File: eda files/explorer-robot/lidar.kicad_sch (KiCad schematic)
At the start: 4 parts, among them J6 LID, Q2 AO3400A

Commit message: Add sheet titles and tidy RP2354B schematic layout
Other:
- title: (none) -> LIDAR connector
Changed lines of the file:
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@@
 	(paper "A4")
 	(title_block
+		(title "LIDAR connector")
 		(date "2026-09-27")
 		(rev "v.0.1")

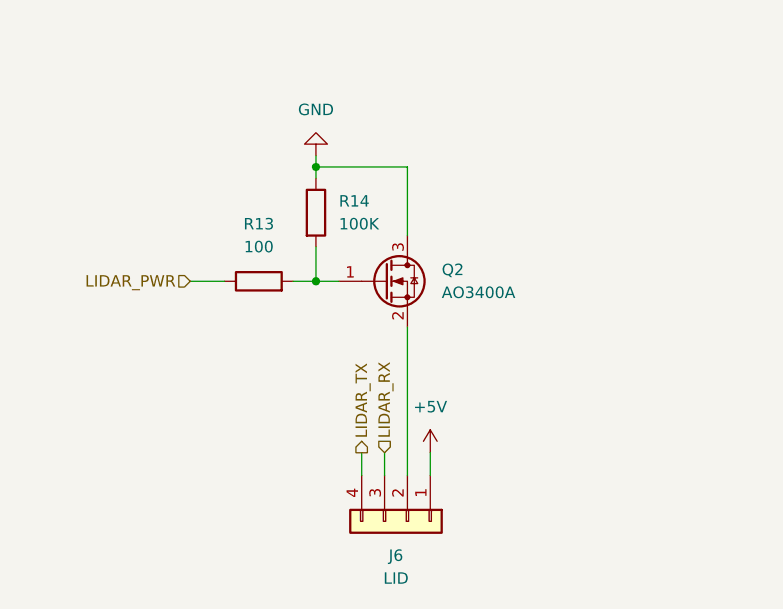
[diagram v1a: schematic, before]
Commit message: Replace power MOSFETs with TPS22917 load switches
Document the switch from low-side MOSFETs to TPS22917 high-side
load switches on the LiDAR and AI camera branches, and add the
expansion connector's switched branch.

Add ADR-0023 requiring each branch's UART to be quiesced and
tri-stated before its power is switched off, to prevent back-feeding
the unpowered load through its ESD diodes.

Rename the `power_mosfet` resource fields to `power_enable`, add
GPIO32 (`EXP_PWR`), and note that the three switched branches can
push the 5 V rail above its continuous current target.
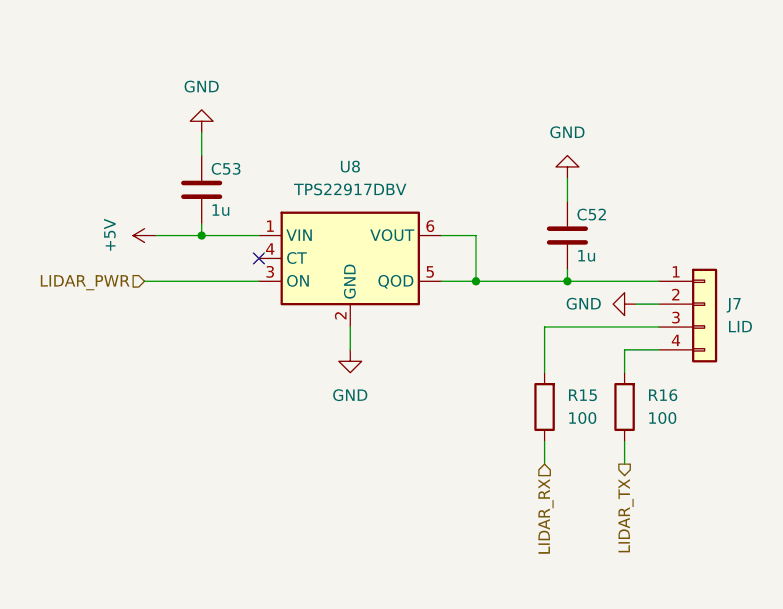
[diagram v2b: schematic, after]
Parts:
- removed J6: LID, Connector_JST:JST_PH_B4B-PH-K_1x04_P2.00mm_Vertical, symbol Connector_Generic:Conn_01x04
- removed Q2: AO3400A, Package_TO_SOT_SMD:SOT-23, symbol Transistor_FET:AO3400A
- removed R13: 100, Resistor_SMD:R_0603_1608Metric, symbol Device:R
- removed R14: 100K, Resistor_SMD:R_0603_1608Metric, symbol Device:R
- added C52, C53: 1u, Capacitor_SMD:C_0603_1608Metric, symbol Device:C
- added J7: LID, Connector_JST:JST_PH_B4B-PH-K_1x04_P2.00mm_Vertical, symbol Connector_Generic:Conn_01x04
- added R15, R16: 100, Resistor_SMD:R_0603_1608Metric, symbol Device:R
- added U8: TPS22917DBV, Package_TO_SOT_SMD:SOT-23-6, symbol Power_Management:TPS22917DBV
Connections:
- net +5V: now also C53.2, U8.1 (VIN)
- net GND: now also C52.1, C53.1, J7.2 (Pin_2), U8.2 (GND)
- net LIDAR_PWR: now also U8.3 (ON)
- net LIDAR_RX: now also R15.1
- net LIDAR_TX: now also R16.1
- new net: J7.4 (Pin_4), R16.2
- new net: C52.2, J7.1 (Pin_1), U8.5 (QOD), U8.6 (VOUT)
- new net: J7.3 (Pin_3), R15.2
- no-connect marks 0 -> 1

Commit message: Add JLCPCB part data for load switch
Also flip BOM sort order to ascending by reference.
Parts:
- U8: JLCPCB_URL (none) -> https://jlcpcb.com/partdetail/TexasInstruments-TPS22917DBVR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; LCSC (none) -> C2681320; MPN (none) -> TPS22917DBVR
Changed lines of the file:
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@@
+			)
+		)
+		(property "JLCPCB_URL" "https://jlcpcb.com/partdetail/TexasInstruments-TPS22917DBVR/C2681320"
+			(at 146.05 88.9 0)
+			(hide yes)
+			(show_name no)
+			(do_not_autoplace no)
+			(effects
+				(font
+					(size 1.27 1.27)
+				)
+			)
+		)
+		(property "LCSC" "C2681320"
+			(at 146.05 88.9 0)
+			(hide yes)
+			(show_name no)
+			(do_not_autoplace no)
+			(effects
+				(font
+					(size 1.27 1.27)
+				)
+			)
+		)
+		(property "MPN" "TPS22917DBVR"
+			(at 146.05 88.9 0)
+			(hide yes)
+			(show_name no)
+			(do_not_autoplace no)
+			(effects
+				(font
+					(size 1.27 1.27)
+				)
 			)
 		)

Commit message: Add R17 current-limiting resistor to lidar schematic
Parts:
- added R17: 100, Resistor_SMD:R_0603_1608Metric, symbol Device:R
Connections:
- net at C52.2, J7.1 (Pin_1), U8.6 (VOUT): now also R17.1; no longer U8.5 (QOD)
- new net: R17.2, U8.5 (QOD)
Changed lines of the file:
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@@
 	)
 	(junction
-		(at 160.02 91.44)
+		(at 165.1 91.44)
 		(diameter 0)
 		(color 0 0 0 0)
@@
 	(wire
 		(pts
-			(xy 156.21 86.36) (xy 160.02 86.36)
+			(xy 156.21 86.36) (xy 165.1 86.36)
 		)
 		(stroke
@@
 	(wire
 		(pts
+			(xy 163.83 91.44) (xy 170.18 91.44)
+		)
+		(stroke
+			(width 0)
+			(type default)
+		)
+	)
+	(wire
+		(pts
 			(xy 170.18 90.17) (xy 170.18 91.44)
 		)
@@
 	(wire
 		(pts
-			(xy 160.02 86.36) (xy 160.02 91.44)
+			(xy 165.1 86.36) (xy 165.1 91.44)
 		)
 		(stroke
@@
 	(wire
 		(pts
-			(xy 160.02 91.44) (xy 156.21 91.44)
-		)
-		(stroke
-			(width 0)
-			(type default)
-		)
-	)
-	(wire
-		(pts
 			(xy 124.46 86.36) (xy 129.54 86.36)
-		)
-		(stroke
-			(width 0)
-			(type default)
-		)
-	)
-	(wire
-		(pts
-			(xy 160.02 91.44) (xy 170.18 91.44)
 		)
 		(stroke
@@
 					(unit 1)
 				)
+			)
+		)
+	)
+	(symbol
+		(lib_id "Device:R")
+		(at 160.02 91.44 270)
+		(unit 1)
+		(body_style 1)
+		(exclude_from_sim no)
+		(in_bom yes)
+		(on_board yes)
+		(in_pos_files yes)
+		(dnp no)
+		(property "Reference" "R17"
+			(at 160.02 93.726 90)
+			(show_name no)
+			(do_not_autoplace no)
+			(effects
+				(font
+					(size 1.27 1.27)
+				)
+			)
+		)
+		(property "Value" "100"
+			(at 160.02 96.266 90)
+			(show_name no)
+			(do_not_autoplace no)
+			(effects
+				(font
+					(size 1.27 1.27)
+				)
+			)
+		)
+		(property "Footprint" "Resistor_SMD:R_0603_1608Metric"
+			(at 160.02 89.662 90)
+			(hide yes)
+			(show_name no)
+			(do_not_autoplace no)
+			(effects
+				(font
+					(size 1.27 1.27)
+				)
+			)
+		)
+		(property "Datasheet" ""
+			(at 160.02 91.44 0)
+			(hide yes)
+			(show_name no)
+			(do_not_autoplace no)
+			(effects
+				(font
+					(size 1.27 1.27)
+				)
+			)
+		)
+		(property "Description" "Resistor"
+			(at 160.02 91.44 0)
+			(hide yes)
+			(show_name no)
+			(do_not_autoplace no)
+			(effects
+				(font
+					(size 1.27 1.27)
+				)
+			)
+		)
+		(property "JLCPCB_URL" "https://jlcpcb.com/partdetail/23502-0603WAF1000T5E/C22775"
+			(at 160.02 91.44 0)
+			(hide yes)
+			(show_name no)
+			(do_not_autoplace no)
+			(effects
+				(font
+					(size 1.27 1.27)
+				)
+			)
+		)
+		(property "LCSC" "C22775"
+			(at 160.02 91.44 0)
+			(hide yes)
+			(show_name no)
+			(do_not_autoplace no)
+			(effects
+				(font
+					(size 1.27 1.27)
+				)
+			)
+		)
+		(property "MFR" "UNI-ROYAL(Uniroyal Elec)"
+			(at 160.02 91.44 0)
+			(hide yes)
+			(show_name no)
+			(do_not_autoplace no)
+			(effects
+				(font
+					(size 1.27 1.27)
+				)
+			)
+		)
+		(property "MPN" "0603WAF1000T5E"
+			(at 160.02 91.44 0)
+			(hide yes)
+			(show_name no)
+			(do_not_autoplace no)
+			(effects
+				(font
+					(size 1.27 1.27)
+				)
+			)
+		)
+		(pin "1"
+		)
+		(pin "2"
+		)
+		(instances
+			(project "explorer-robot"
+				(path "/57778957-dc0c-4e39-b470-8f64ada5e845/59ee77a0-3af7-4f56-bf2b-31c06f43662c"
+					(reference "R17")
+					(unit 1)
+				)

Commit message: ``` Move AI camera branch to 3.3 V rail
The Grove Vision AI V2 module used here requires a 3.3 V input,
so powering it from the switched 5 V branch would over-voltage it.
Point U9 VIN at +3.3V; the TPS22917, footprint and control are
unchanged.

Also bump the 5 V inductor to 15 µH/3 A, swap the catch diode,
clean up schematic wiring and add no-connects on unused pins.
Document the decision in ADR-0025 and update ADR-0019, ADR-0021
and CONTEXT.md.
```
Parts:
- added C40: 10u, Capacitor_SMD:C_0805_2012Metric, symbol Device:C
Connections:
- net GND: now also C40.2
- net at C52.2, J7.1 (Pin_1), R17.1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: now also C40.1
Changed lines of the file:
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@@
+		(color 0 0 0 0)
+	)
+	(junction
+		(at 179.07 91.44)
+		(diameter 0)
 		(color 0 0 0 0)
 	)
@@
 	(wire
 		(pts
+			(xy 179.07 91.44) (xy 180.34 91.44)
+		)
+		(stroke
+			(width 0)
+			(type default)
+		)
+	)
+	(wire
+		(pts
 			(xy 170.18 80.01) (xy 170.18 82.55)
 		)
@@
 	(wire
 		(pts
+			(xy 179.07 90.17) (xy 179.07 91.44)
+		)
+		(stroke
+			(width 0)
+			(type default)
+		)
+	)
+	(wire
+		(pts
 			(xy 176.53 99.06) (xy 180.34 99.06)
 		)
@@
 	(wire
 		(pts
-			(xy 170.18 91.44) (xy 180.34 91.44)
+			(xy 170.18 91.44) (xy 179.07 91.44)
+		)
+		(stroke
+			(width 0)
+			(type default)
+		)
+	)
+	(wire
+		(pts
+			(xy 179.07 80.01) (xy 179.07 82.55)
 		)
 		(stroke
@@
 	)
 	(symbol
+		(lib_id "power:GND")
+		(at 179.07 80.01 180)
+		(unit 1)
+		(body_style 1)
+		(exclude_from_sim no)
+		(in_bom yes)
+		(on_board yes)
+		(in_pos_files yes)
+		(dnp no)
+		(fields_autoplaced yes)
+		(property "Reference" "#PWR093"
+			(at 179.07 73.66 0)
+			(hide yes)
+			(show_name no)
+			(do_not_autoplace no)
+			(effects
+				(font
+					(size 1.27 1.27)
+				)
+			)
+		)
+		(property "Value" "GND"
+			(at 179.07 74.93 0)
+			(show_name no)
+			(do_not_autoplace no)
+			(effects
+				(font
+					(size 1.27 1.27)
+				)
+			)
+		)
+		(property "Footprint" ""
+			(at 179.07 80.01 0)
+			(hide yes)
+			(show_name no)
+			(do_not_autoplace no)
+			(effects
+				(font
+					(size 1.27 1.27)
+				)
+			)
+		)
+		(property "Datasheet" ""
+			(at 179.07 80.01 0)
+			(hide yes)
+			(show_name no)
+			(do_not_autoplace no)
+			(effects
+				(font
+					(size 1.27 1.27)
+				)
+			)
+		)
+		(property "Description" "Power symbol creates a global label with name \"GND\" , ground"
+			(at 179.07 80.01 0)
+			(hide yes)
+			(show_name no)
+			(do_not_autoplace no)
+			(effects
+				(font
+					(size 1.27 1.27)
+				)
+			)
+		)
+		(pin "1"
+		)
+		(instances
+			(project "explorer-robot"
+				(path "/57778957-dc0c-4e39-b470-8f64ada5e845/59ee77a0-3af7-4f56-bf2b-31c06f43662c"
+					(reference "#PWR093")
+					(unit 1)
+				)
+			)
+		)
+	)
+	(symbol
 		(lib_id "Connector_Generic:Conn_01x04")
 		(at 185.42 93.98 0)
@@
 					(unit 1)
 				)
+			)
+		)
+	)
+	(symbol
+		(lib_id "Device:C")
+		(at 179.07 86.36 180)
+		(unit 1)
+		(body_style 1)
+		(exclude_from_sim no)
+		(in_bom yes)
+		(on_board yes)
+		(in_pos_files yes)
+		(dnp no)
+		(property "Reference" "C40"
+			(at 186.182 87.376 0)
+			(show_name no)
+			(do_not_autoplace no)
+			(effects
+				(font
+					(size 1.27 1.27)
+				)
+				(justify left)
+			)
+		)
+		(property "Value" "10u"
+			(at 186.182 84.836 0)
+			(show_name no)
+			(do_not_autoplace no)
+			(effects
+				(font
+					(size 1.27 1.27)
+				)
+				(justify left)
+			)
+		)
+		(property "Footprint" "Capacitor_SMD:C_0805_2012Metric"
+			(at 178.1048 82.55 0)
+			(hide yes)
+			(show_name no)
+			(do_not_autoplace no)
+			(effects
+				(font
+					(size 1.27 1.27)
+				)
+			)
+		)
+		(property "Datasheet" ""
+			(at 179.07 86.36 0)
+			(hide yes)
+			(show_name no)
+			(do_not_autoplace no)
+			(effects
+				(font
+					(size 1.27 1.27)
+				)
+			)
+		)
+		(property "Description" "Unpolarized capacitor"
+			(at 179.07 86.36 0)
+			(hide yes)
+			(show_name no)
+			(do_not_autoplace no)
+			(effects
+				(font
+					(size 1.27 1.27)
+				)
+			)
+		)
+		(property "JLCPCB_URL" "https://jlcpcb.com/partdetail/16532-CL21A106KAYNNNE/C15850"
+			(at 179.07 86.36 0)
+			(hide yes)
+			(show_name no)
+			(do_not_autoplace no)
+			(effects
+				(font
+					(size 1.27 1.27)
+				)
+			)
+		)
+		(property "LCSC" "C15850"
+			(at 179.07 86.36 0)
+			(hide yes)
+			(show_name no)
+			(do_not_autoplace no)
+			(effects
+				(font
+					(size 1.27 1.27)
+				)
+			)
+		)
+		(property "MFR" "Samsung Electro-Mechanics"
+			(at 179.07 86.36 0)
+			(hide yes)
+			(show_name no)
+			(do_not_autoplace no)
+			(effects
+				(font
+					(size 1.27 1.27)
+				)
+			)
+		)
+		(property "MPN" "CL21A106KAYNNNE"
+			(at 179.07 86.36 0)
+			(hide yes)
+			(show_name no)
+			(do_not_autoplace no)
+			(effects
+				(font
+					(size 1.27 1.27)
+				)
+			)
+		)
+		(pin "2"
+		)
+		(pin "1"
+		)
+		(instances
+			(project "explorer-robot"
+				(path "/57778957-dc0c-4e39-b470-8f64ada5e845/59ee77a0-3af7-4f56-bf2b-31c06f43662c"
+					(reference "C40")
+					(unit 1)
+				)

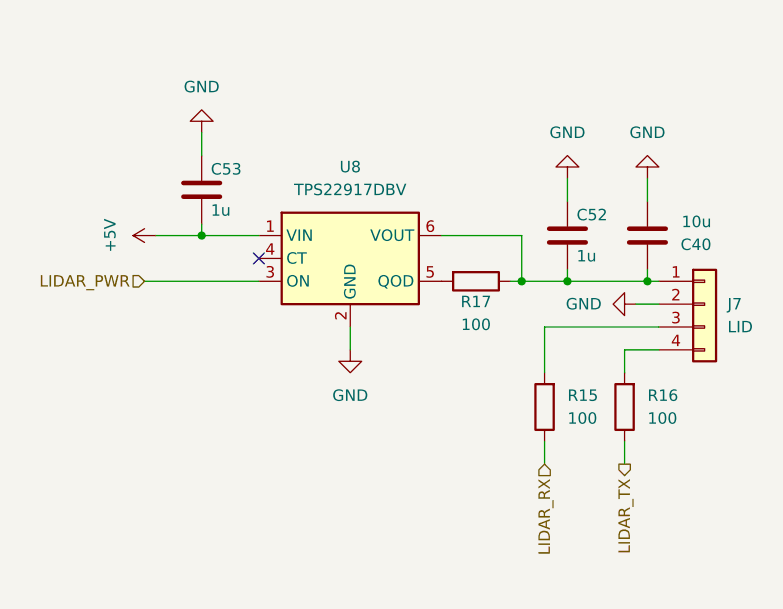
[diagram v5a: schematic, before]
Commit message: Add 1 nF CT capacitors to TPS22917 load switches
Specify C29/C30/C67/C68 on the LiDAR, AI camera, expansion and
panel branches to give a controlled rise and limit inrush. Update
ADRs 0010, 0021, 0024 and 0027 and CONTEXT.md to match, rework the
affected schematics, and swap the inductor footprint to the
EasyEDA SLO0618H part.
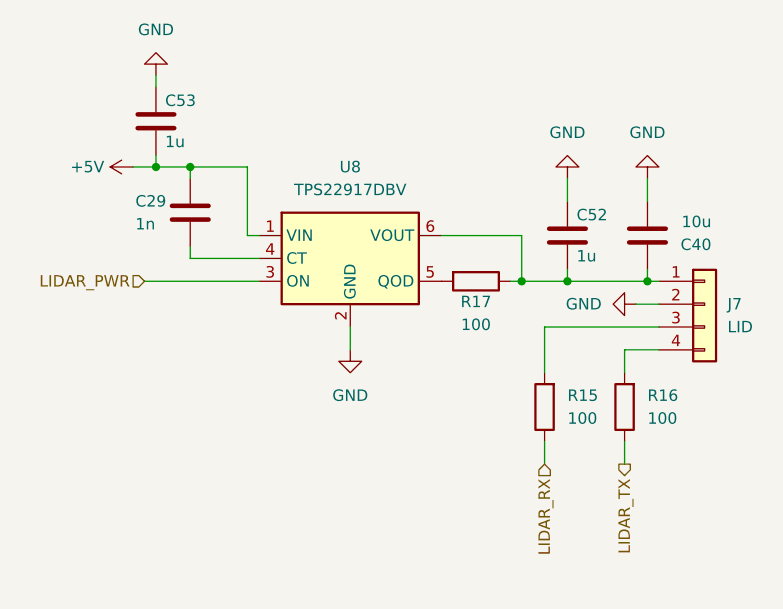
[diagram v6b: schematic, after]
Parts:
- added C29: 1n, Capacitor_SMD:C_0603_1608Metric, symbol Device:C
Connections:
- net +5V: now also C29.2
- net at U8.4 (CT): now also C29.1
- no-connect marks 1 -> 0
